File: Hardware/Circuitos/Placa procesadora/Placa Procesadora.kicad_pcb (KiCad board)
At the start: 2 copper layers, 46 x 45 mm, 26 parts, among them J1 Conn_01x02, J2 Conn_01x02, J7 Conn_01x02, U1 LM358

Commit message: Placa procesadora - Borde de placa
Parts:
- removed C1: 1nF, Capacitor_THT:C_Radial_D5.0mm_H11.0mm_P2.00mm
- removed C2: 390pF, Capacitor_THT:C_Radial_D5.0mm_H11.0mm_P2.00mm
- removed C3, C5, C8, C9: 100nF, Capacitor_THT:C_Radial_D5.0mm_H11.0mm_P2.00mm
- removed C4, C6, C7: 10uF, Capacitor_THT:C_Radial_D5.0mm_H11.0mm_P2.00mm
- removed D5: BAT-85, Diode_THT:D_DO-35_SOD27_P7.62mm_Horizontal
- removed J1, J2, J7: Conn_01x02, Connector_Molex:Molex_KK-254_AE-6410-02A_1x02_P2.54mm_Vertical
- removed R1: 3.9K, Resistor_THT:R_Axial_DIN0204_L3.6mm_D1.6mm_P7.62mm_Horizontal
- removed R10: 1M, Resistor_THT:R_Axial_DIN0204_L3.6mm_D1.6mm_P7.62mm_Horizontal
- removed R11: 100k, Resistor_THT:R_Axial_DIN0204_L3.6mm_D1.6mm_P7.62mm_Horizontal
- removed R13: 100K, Resistor_THT:R_Axial_DIN0204_L3.6mm_D1.6mm_P7.62mm_Horizontal
- removed R2, R5, R6: 10K, Resistor_THT:R_Axial_DIN0204_L3.6mm_D1.6mm_P7.62mm_Horizontal
- removed R3, R7, R8: 1K, Resistor_THT:R_Axial_DIN0204_L3.6mm_D1.6mm_P7.62mm_Horizontal
- removed R4, R9: 2.2K, Resistor_THT:R_Axial_DIN0204_L3.6mm_D1.6mm_P7.62mm_Horizontal
- removed U1: LM358, Package_DIP:DIP-8_W7.62mm
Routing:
- net /5V: track 67.6 -> 0.00 mm
- net Net-(R4-Pad2): track 55.4 -> 0.00 mm
- net Net-(C4-Pad1): track 23.1 -> 0.00 mm
- net Net-(C8-Pad1): track 22.2 -> 0.00 mm
- net Net-(D5-K): track 22.1 -> 0.00 mm
- net Net-(U1A-+): track 21.7 -> 0.00 mm
- net Net-(U1A--): track 21.5 -> 0.00 mm
- net Net-(D5-A): track 14.2 -> 0.00 mm
- net Net-(U1B--): track 14.0 -> 0.00 mm
- net Net-(C1-Pad1): track 12.8 -> 0.00 mm
- net Net-(C2-Pad2): track 12.7 -> 0.00 mm
- net Net-(C6-Pad1): track 11.7 -> 0.00 mm
- net Net-(C7-Pad1): track 8.93 -> 0.00 mm
- net Net-(J1-Pin_1): track 6.31 -> 0.00 mm
- net Net-(U1B-+): track 6.20 -> 0.00 mm
- removed copper zone on B.Cu, net Earth

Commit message: Placa procesadora - Componentes en PCB
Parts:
- added C1: 1nF, Capacitor_THT:C_Radial_D5.0mm_H11.0mm_P2.00mm, F.Cu at (127.0, 42.8)
- added C2: 390pF, Capacitor_THT:C_Radial_D5.0mm_H11.0mm_P2.00mm, F.Cu at (133.6, 43.6)
- added C3: 100nF, Capacitor_THT:C_Radial_D5.0mm_H11.0mm_P2.00mm, F.Cu at (144.8, 37.6)
- added C4: 10uF, Capacitor_THT:C_Radial_D5.0mm_H11.0mm_P2.00mm, F.Cu at (151.4, 57.2)
- added C5: 100nF, Capacitor_THT:C_Radial_D5.0mm_H11.0mm_P2.00mm, F.Cu at (144.4, 58.8)
- added C6: 10uF, Capacitor_THT:C_Radial_D5.0mm_H11.0mm_P2.00mm, F.Cu at (147.8, 66.2)
- added C7: 10uF, Capacitor_THT:C_Radial_D5.0mm_H11.0mm_P2.00mm, F.Cu at (126.0, 70.0)
- added C8: 100nF, Capacitor_THT:C_Radial_D5.0mm_H11.0mm_P2.00mm, F.Cu at (119.4, 68.8)
- added C9: 100nF, Capacitor_THT:C_Radial_D5.0mm_H11.0mm_P2.00mm, F.Cu at (137.2, 76.2)
- added D5: BAT-85, Diode_THT:D_DO-35_SOD27_P7.62mm_Horizontal, F.Cu at (128.8, 76.8)
- added J1: Conn_01x02, Connector_Molex:Molex_KK-254_AE-6410-02A_1x02_P2.54mm_Vertical, F.Cu at (115.4, 39.3)
- added J2: Conn_01x02, Connector_Molex:Molex_KK-254_AE-6410-02A_1x02_P2.54mm_Vertical, F.Cu at (150.4, 76.8)
- added J7: Conn_01x02, Connector_Molex:Molex_KK-254_AE-6410-02A_1x02_P2.54mm_Vertical, F.Cu at (152.2, 40.2)
- added R1: 3.9K, Resistor_THT:R_Axial_DIN0204_L3.6mm_D1.6mm_P7.62mm_Horizontal, F.Cu at (121.0, 37.6)
- added R10: 1M, Resistor_THT:R_Axial_DIN0204_L3.6mm_D1.6mm_P7.62mm_Horizontal, F.Cu at (143.2, 76.4)
- added R11: 100k, Resistor_THT:R_Axial_DIN0204_L3.6mm_D1.6mm_P7.62mm_Horizontal, F.Cu at (114.6, 76.2)
- added R13: 100K, Resistor_THT:R_Axial_DIN0204_L3.6mm_D1.6mm_P7.62mm_Horizontal, F.Cu at (143.4, 52.4)
- added R2: 10K, Resistor_THT:R_Axial_DIN0204_L3.6mm_D1.6mm_P7.62mm_Horizontal, F.Cu at (132.2, 37.6)
- added R3: 1K, Resistor_THT:R_Axial_DIN0204_L3.6mm_D1.6mm_P7.62mm_Horizontal, F.Cu at (138.6, 52.6)
- added R4: 2.2K, Resistor_THT:R_Axial_DIN0204_L3.6mm_D1.6mm_P7.62mm_Horizontal, F.Cu at (135.4, 65.6)
- added R5: 10K, Resistor_THT:R_Axial_DIN0204_L3.6mm_D1.6mm_P7.62mm_Horizontal, F.Cu at (152.4, 44.8)
- added R6: 10K, Resistor_THT:R_Axial_DIN0204_L3.6mm_D1.6mm_P7.62mm_Horizontal, F.Cu at (148.2, 44.8)
- added R7: 1K, Resistor_THT:R_Axial_DIN0204_L3.6mm_D1.6mm_P7.62mm_Horizontal, F.Cu at (119.2, 45.6)
- added R8: 1K, Resistor_THT:R_Axial_DIN0204_L3.6mm_D1.6mm_P7.62mm_Horizontal, F.Cu at (119.2, 56.8)
- added R9: 2.2K, Resistor_THT:R_Axial_DIN0204_L3.6mm_D1.6mm_P7.62mm_Horizontal, F.Cu at (114.8, 52.2)
- added U1: LM358, Package_DIP:DIP-8_W7.62mm, F.Cu at (132.4, 59.4)

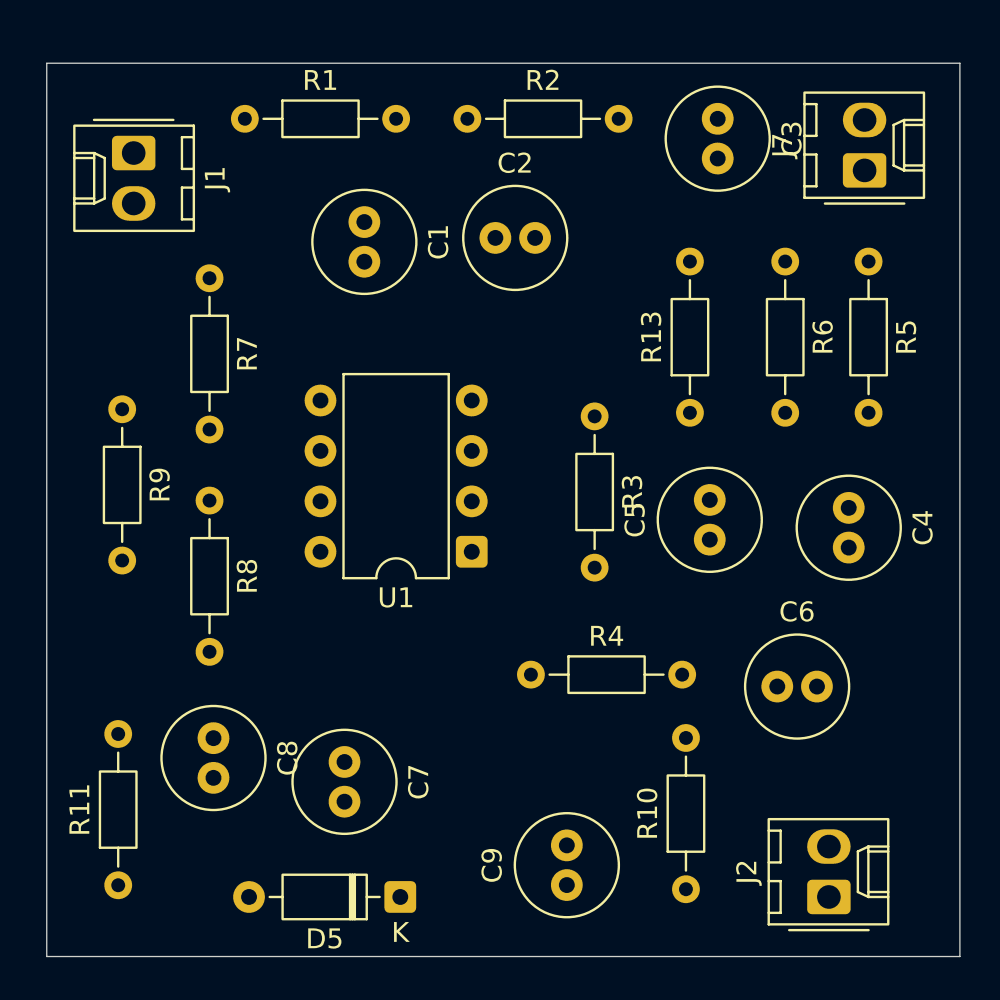
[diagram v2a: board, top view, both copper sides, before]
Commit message: Placa procesadora - Conexión componentes PCB
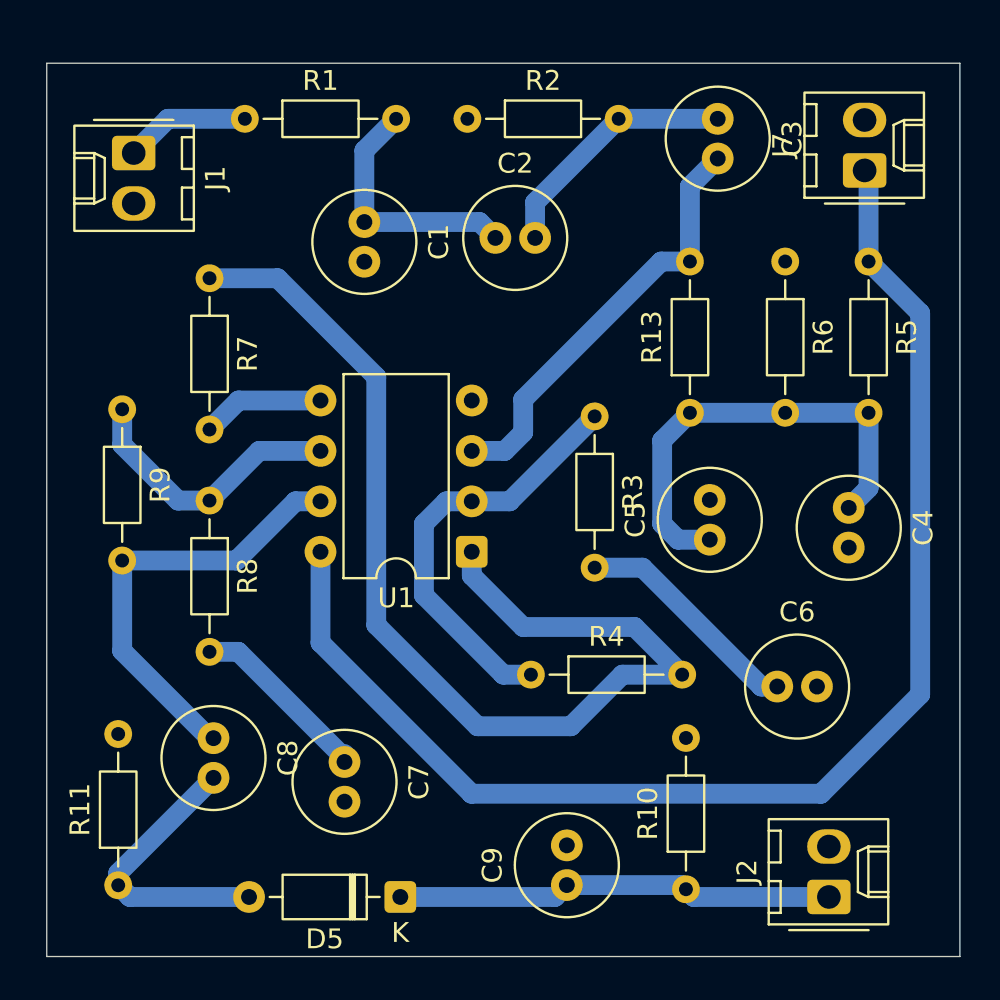
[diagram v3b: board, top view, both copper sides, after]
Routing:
- net /5V: track 0.00 -> 67.6 mm
- net Net-(R4-Pad2): track 0.00 -> 55.4 mm
- net Net-(C4-Pad1): track 0.00 -> 23.1 mm
- net Net-(C8-Pad1): track 0.00 -> 22.2 mm
- net Net-(D5-K): track 0.00 -> 22.1 mm
- net Net-(U1A-+): track 0.00 -> 21.7 mm
- net Net-(U1A--): track 0.00 -> 21.5 mm
- net Net-(D5-A): track 0.00 -> 14.2 mm
- net Net-(U1B--): track 0.00 -> 14.0 mm
- net Net-(C1-Pad1): track 0.00 -> 12.8 mm
- net Net-(C2-Pad2): track 0.00 -> 12.7 mm
- net Net-(C6-Pad1): track 0.00 -> 11.7 mm
- net Net-(C7-Pad1): track 0.00 -> 8.93 mm
- net Net-(J1-Pin_1): track 0.00 -> 6.31 mm
- net Net-(U1B-+): track 0.00 -> 6.20 mm

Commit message: Placa procesadora - Zona de tierra PCB
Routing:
- added copper zone on B.Cu, net Earth
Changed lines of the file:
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@@
 		(net "Net-(U1B-+)")
+	)
+	(zone
+		(net "Earth")
+		(layer "B.Cu")
+		(hatch edge 0.5)
+		(connect_pads
+			(clearance 0.5)
+		)
+		(min_thickness 0.25)
+		(fill yes
+			(thermal_gap 0.5)
+			(thermal_bridge_width 0.5)
+			(island_removal_mode 0)
+		)
+		(polygon
+			(pts
+				(xy 157 34.8) (xy 111 34.8) (xy 111 79.8) (xy 157 79.8)
+			)
+		)
 	)
 	(embedded_fonts no)

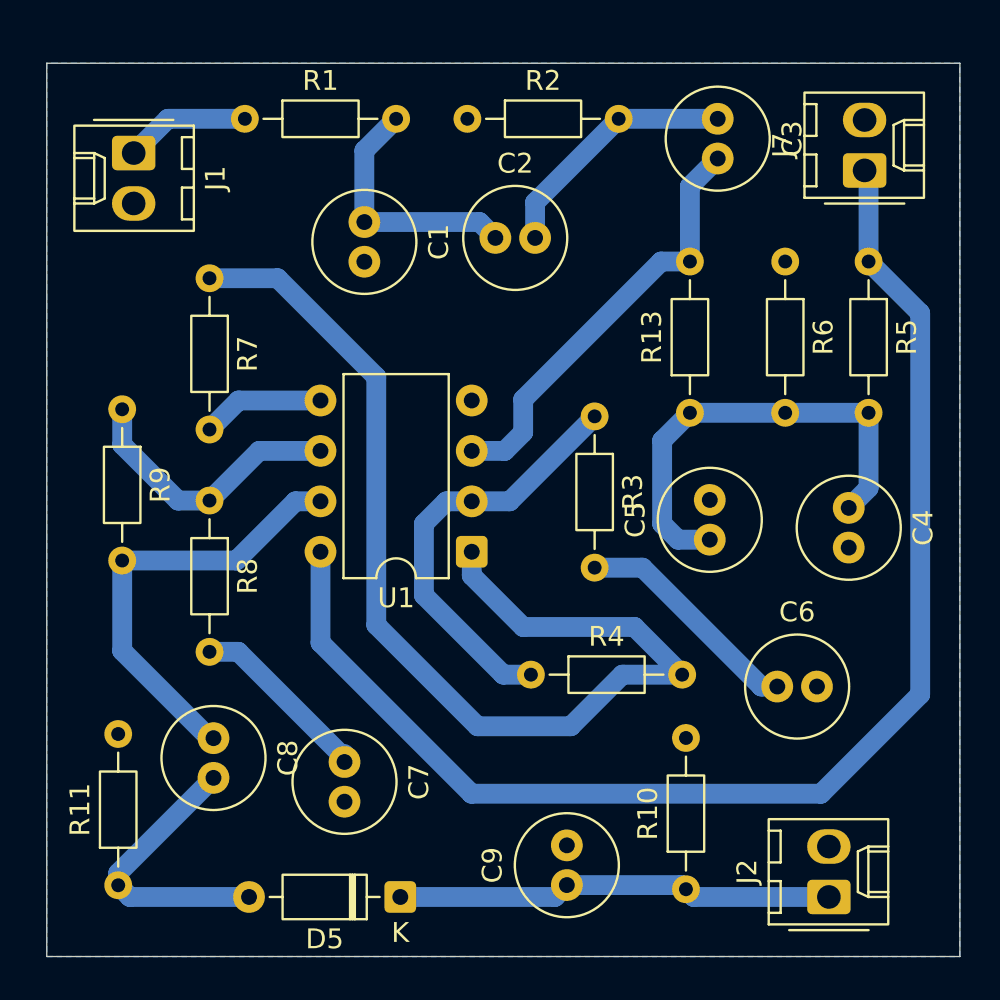
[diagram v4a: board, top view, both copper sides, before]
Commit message: Placa procesadora - Acomodar componentes
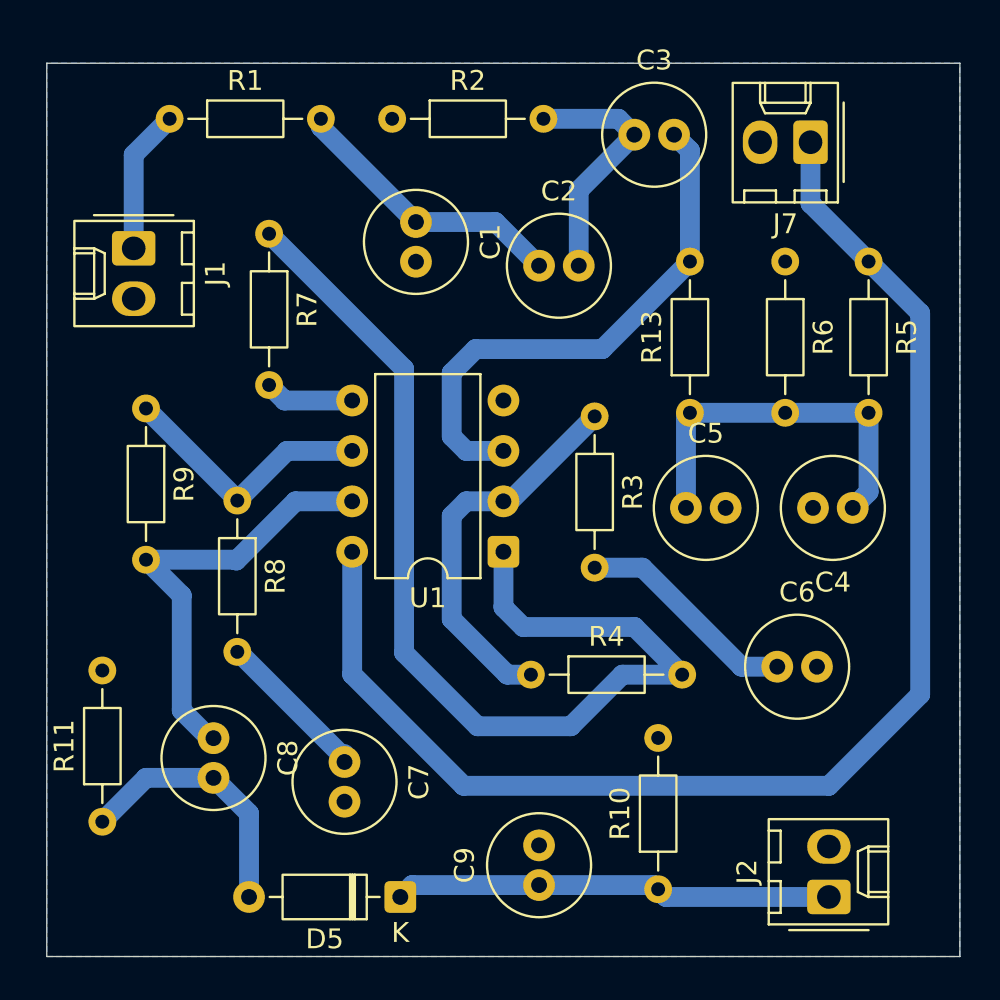
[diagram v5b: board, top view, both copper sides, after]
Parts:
- moved J1 4.80 mm to (115.4, 44.1)
- moved C3 4.28 mm to (140.6, 38.4), turned to 0 degrees
- moved R1 3.79 mm to (117.2, 37.6)
- moved R2 3.79 mm to (128.4, 37.6)
- moved R7 3.74 mm to (122.2, 43.4)
- moved R11 3.30 mm to (113.8, 73.0)
- moved J7 3.07 mm to (149.5, 38.8), turned to 180 degrees
- moved C2 2.61 mm to (135.8, 45.0)
- moved C1 2.60 mm to (129.6, 42.8)
- moved C5 2.00 mm to (143.2, 57.2), turned to 0 degrees
- moved U1 1.59 mm to (134.0, 59.4)
- moved R8 1.40 mm to (120.6, 56.8)
- moved C9 1.40 mm to (135.8, 76.2)
- moved R10 1.40 mm to (141.8, 76.4)
- moved R9 1.20 mm to (116.0, 52.2)
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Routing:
- net Net-(U1A-+): track 21.7 -> 27.4 mm
- net Net-(C4-Pad1): track 23.1 -> 19.0 mm
- net Net-(U1A--): track 21.5 -> 19.3 mm
- net Net-(U1B-+): track 6.20 -> 4.51 mm
- net Net-(R4-Pad2): track 55.4 -> 53.8 mm
- net /5V: track 67.6 -> 69.1 mm
- net Net-(C1-Pad1): track 12.8 -> 14.3 mm
- net Net-(C7-Pad1): track 8.93 -> 7.48 mm
- net Net-(D5-A): track 14.2 -> 13.3 mm
- net Net-(J1-Pin_1): track 6.31 -> 7.27 mm
- net Net-(U1B--): track 14.0 -> 13.4 mm

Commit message: Placa procesadora - Muescas para placas
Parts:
- moved R7 8.62 mm to (129.6, 47.8), turned to 180 degrees
- moved R1 8.08 mm to (121.2, 44.6), turned to 90 degrees
- moved J2 7.67 mm to (152.4, 69.4)
- moved R11 4.60 mm to (113.6, 68.4)
- moved C6 4.29 mm to (144.0, 63.2)
- moved R2 3.21 mm to (125.2, 37.6)
- moved C3 2.83 mm to (137.8, 38.0), turned to -90 degrees
- moved J1 2.40 mm to (115.4, 46.5)
- moved J7 2.28 mm to (147.2, 38.8)
- moved C2 2.21 mm to (133.6, 45.2)
- moved R4 1.80 mm to (133.6, 65.6)
- moved R9 1.72 mm to (117.0, 53.6)
- moved R10 1.61 mm to (143.4, 76.2)
- moved C1 1.52 mm to (128.2, 42.2)
- moved D5 1.26 mm to (130.0, 76.4)
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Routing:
- net Net-(R4-Pad2): track 53.8 -> 39.4 mm
- net Net-(C6-Pad1): track 11.3 -> 6.64 mm
- net Net-(U1B-+): track 4.51 -> 7.81 mm
- net Net-(D5-K): track 22.1 -> 25.3 mm
- net Net-(C1-Pad1): track 14.3 -> 16.7 mm
- net Net-(C8-Pad1): track 22.2 -> 19.9 mm
- net /5V: track 69.1 -> 67.5 mm
- net Net-(U1B--): track 13.4 -> 11.8 mm
- net Net-(C2-Pad2): track 12.7 -> 13.9 mm
- net Net-(U1A-+): track 27.4 -> 28.2 mm
- net Net-(J1-Pin_1): track 7.27 -> 6.61 mm
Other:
- outline, holes or cut-outs redrawn

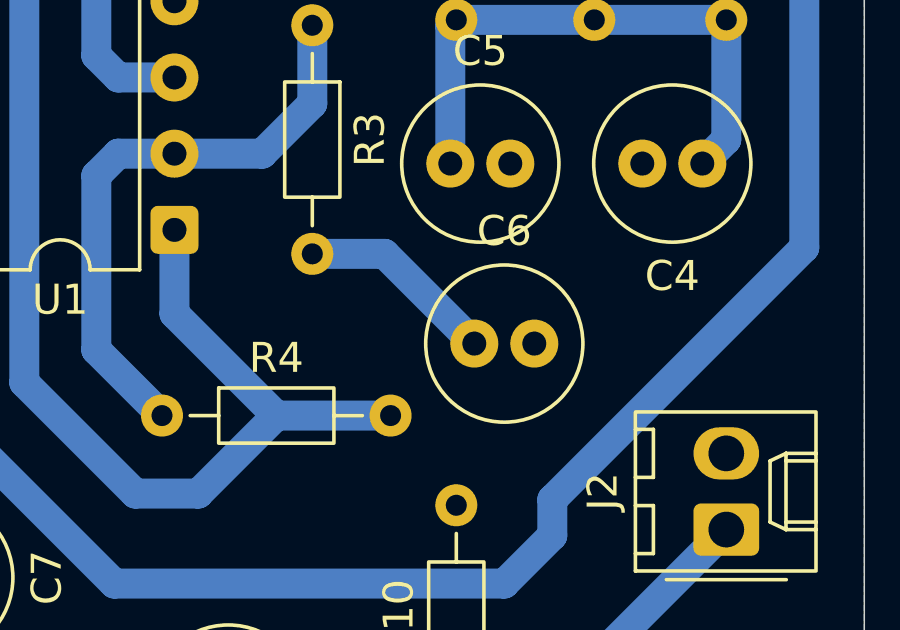
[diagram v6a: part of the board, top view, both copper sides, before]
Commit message: Placa procesadora - Arreglar margenes de tierra
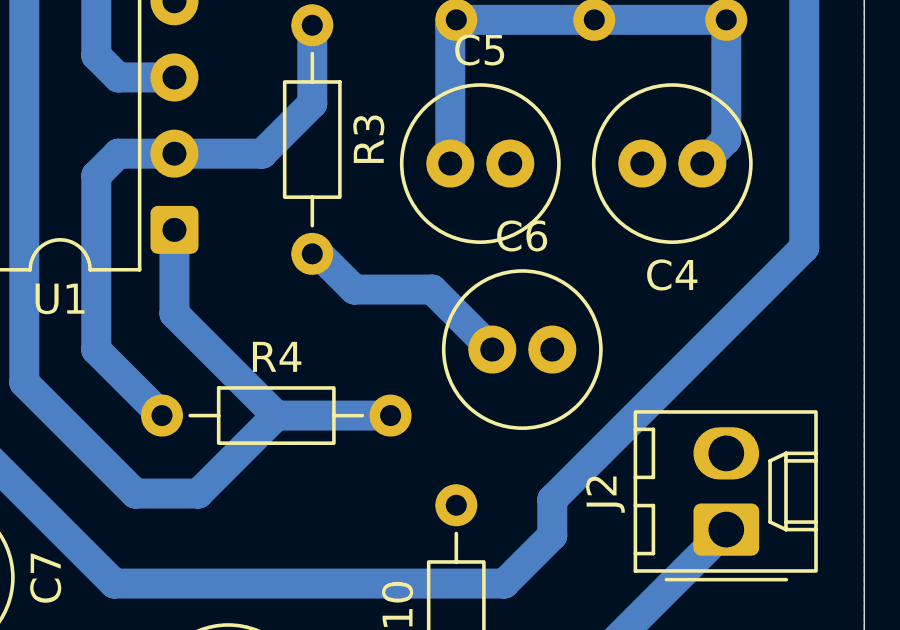
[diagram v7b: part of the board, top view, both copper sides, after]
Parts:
- moved C6 0.63 mm to (144.6, 63.4)
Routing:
- net Net-(C6-Pad1): track 6.64 -> 7.32 mm
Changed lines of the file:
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@@
 	(footprint "Capacitor_THT:C_Radial_D5.0mm_H11.0mm_P2.00mm"
 		(layer "F.Cu")
-		(at 144 63.2)
+		(at 144.6 63.4)
 		(descr "C, Radial series, Radial, pin pitch=2.00mm, diameter=5mm, height=11mm, Non-Polar Electrolytic Capacitor")
 		(tags "C Radial series Radial pin pitch 2.00mm diameter 5mm height 11mm Non-Polar Electrolytic Capacitor")
@@
 	)
 	(segment
-		(start 141.01 60.21)
+		(start 144.6 63.4)
+		(end 142.6 61.4)
+		(width 1)
+		(layer "B.Cu")
+		(net "Net-(C6-Pad1)")
+	)
+	(segment
+		(start 142.6 61.4)
+		(end 140 61.4)
+		(width 1)
+		(layer "B.Cu")
+		(net "Net-(C6-Pad1)")
+	)
+	(segment
+		(start 138.81 60.21)
 		(end 138.6 60.21)
 		(width 1)
@@
 	)
 	(segment
-		(start 144 63.2)
-		(end 141.01 60.21)
+		(start 140 61.4)
+		(end 138.81 60.21)
 		(width 1)
 		(layer "B.Cu")
@@
 		(hatch edge 0.5)
 		(connect_pads
-			(clearance 0.9)
+			(clearance 0.5)
 		)
 		(min_thickness 0.25)

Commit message: Placa procesadora - Acomodar una pista
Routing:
- net Net-(U1A-+): track 28.2 -> 26.8 mm
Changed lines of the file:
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@@
+	)
+	(segment
+		(start 141.19 44.79)
+		(end 137.38 48.6)
+		(width 1)
+		(layer "B.Cu")
+		(net "Net-(U1A-+)")
 	)
 	(segment
 		(start 131.4 53.6)
 		(end 132.13 54.33)
+		(width 1)
+		(layer "B.Cu")
+		(net "Net-(U1A-+)")
+	)
+	(segment
+		(start 133.2 48.6)
+		(end 131.4 50.4)
+		(width 1)
+		(layer "B.Cu")
+		(net "Net-(U1A-+)")
+	)
+	(segment
+		(start 131.4 50.4)
+		(end 131.4 53.6)
+		(width 1)
+		(layer "B.Cu")
+		(net "Net-(U1A-+)")
+	)
+	(segment
+		(start 137.38 48.6)
+		(end 133.2 48.6)
+		(width 1)
+		(layer "B.Cu")
+		(net "Net-(U1A-+)")
+	)
+	(segment
+		(start 143.4 44.79)
+		(end 143.4 45)
 		(width 1)
 		(layer "B.Cu")
@@
 	(segment
 		(start 137.8 40)
-		(end 138.61 40)
+		(end 137.8 41.4)
 		(width 1)
 		(layer "B.Cu")
@@
 	)
 	(segment
-		(start 143.4 44.79)
-		(end 138.99 49.2)
+		(start 137.8 41.4)
+		(end 141.19 44.79)
 		(width 1)
 		(layer "B.Cu")
@@
 	)
 	(segment
-		(start 131.4 50.4)
-		(end 131.4 53.6)
-		(width 1)
-		(layer "B.Cu")
-		(net "Net-(U1A-+)")
-	)
-	(segment
-		(start 138.61 40)
+		(start 141.19 44.79)
 		(end 143.4 44.79)
 		(width 1)
 		(layer "B.Cu")
-		(net "Net-(U1A-+)")
-	)
-	(segment
-		(start 138.99 49.2)
-		(end 132.6 49.2)
-		(width 1)
-		(layer "B.Cu")
-		(net "Net-(U1A-+)")
-	)
-	(segment
-		(start 143.4 44.79)
-		(end 143.4 45)
-		(width 1)
-		(layer "B.Cu")
-		(net "Net-(U1A-+)")
-	)
-	(segment
-		(start 132.6 49.2)
-		(end 131.4 50.4)
-		(width 1)
-		(layer "B.Cu")
